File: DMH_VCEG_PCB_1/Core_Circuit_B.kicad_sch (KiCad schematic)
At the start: 98 parts, among them Q1 BC558, Q2 BC548, Q3 BC548, SW1 SW_DPDT_x2, U1 TL074, U2 4001, U3 40106, U4 CD4066BE, U5 TL074, U6 TL074, U7 TL074

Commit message: Placed Circuit B pages
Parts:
- renumbered C18 to C33, C17 to C34, C19 to C35, C20 to C36, C21 to C37, C22 to C38, C24 to C39, C25 to C40, C23 to C41, D3 to D15, D4 to D16, D5 to D17, D6 to D18, D7 to D19, D8 to D20, Q2 to Q5, Q1 to Q6, Q3 to Q7, R73 to R10, R75 to R12, R77 to R14, R74 to R16, R79 to R17, R76 to R18, R101 to R19, R80 to R20, R82 to R21, R100 to R22, R86 to R23, R99 to R24, R81 to R25, R93 to R26, R83 to R27, R98 to R28, R84 to R29, R97 to R30, R95 to R31, R103 to R32, R102 to R33, R91 to R34, R90 to R35, R89 to R36, R94 to R37, R96 to R38, R88 to R39, R92 to R40, R109 to R41, R104 to R42, R105 to R43, R110 to R44, R87 to R45, R106 to R46, R111 to R47, R112 to R48, R107 to R49, R108 to R50, R113 to R51, R114 to R52, R115 to R53, R85 to R54, R72 to R7, R78 to R8, RV23 to RV31, RV25 to RV32, RV26 to RV33, RV19 to RV34, RV18 to RV35, RV20 to RV36, RV27 to RV37, RV21 to RV38, RV24 to RV39, RV22 to RV40, RV17 to RV41, RV28 to RV42, RV29 to RV43, RV30 to RV44, SW1 to SW3, U1 to U11, U4 to U12, U6 to U13, U3 to U14, U2 to U15, U5 to U16, U7 to U17
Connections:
- net Att Logic: now also U12.5, U15.12, U15.4, U15.8; no longer U12.13, U15.1, U15.1, U15.3
- net Dec Logic: now also U15.10; no longer U15.3
- net GND: now also U13.10 (+), U13.5 (+), U17.5 (+); no longer U13.3 (+), U13.3 (+), U17.3 (+)
- net Main Cap: now also U12.4, U12.8; no longer U12.1, U12.1
- net Rel Logic: now also U12.6, U15.11; no longer U12.13, U15.3
- net Sus Level: now also U13.13 (-), U13.14; no longer U13.1, U13.2 (-)
- net at C41.2, R54.2, RV41.1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: now also U16.12 (+); no longer U16.3 (+)
- net at D17.2 (A), U14.2: now also U14.13, U15.9; no longer U14.1, U15.2
- net at Q7.1 (C): now also U12.9; no longer U12.2
- net at R26.1, R28.1, R30.2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: now also U13.6 (-); no longer U13.2 (-)
- net at C39.1, C40.1, R33.1: now also U16.5 (+); no longer U16.3 (+)
- net at R22.1, R23.1, R24.2: now also U13.9 (-); no longer U13.2 (-)
- net at C34.1, R10.1, R16.2: now also U11.5 (+); no longer U11.3 (+)
- net at R46.1, R49.1, R50.2: now also U17.6 (-); no longer U17.2 (-)
- net at C33.2, R12.1, R18.2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: now also U11.6 (-); no longer U11.2 (-)
- net at R24.1, R26.2: now also U13.7; no longer U13.1
- net at R19.1, R22.2: now also U13.8; no longer U13.1
- net at R43.1, R46.2: now also U17.7; no longer U17.1
- net at D19.1 (K), R32.2: now also U13.12 (+); no longer U13.3 (+)
- net at U15.3: now also U15.5; no longer U15.1
- net at C38.2, D18.1 (K), R29.2: now also U15.6; no longer U15.2
- net at Q6.1 (C): now also U12.3; no longer U12.2
- net at C34.2, D15.2 (A), R16.1: now also U11.7; no longer U11.1
- net at D18.2 (A): now also U16.8; no longer U16.1
- new net: R45.2, U16.10 (+), U16.6 (-), U16.7
- new net: Q6.3 (E), U16.13 (-), U16.14, U16.9 (-)
- new net: U14.12, U15.13

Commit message: Reanotated schematic
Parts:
- SW2: renamed from SW3; footprint (none) -> SynthStuff:Toggle_Switch_2_Poles_TE
- U11: footprint (none) -> Package_DIP:DIP-14_W7.62mm_Socket
- U12: renamed from U17; footprint (none) -> Package_DIP:DIP-14_W7.62mm_Socket
- U14: renamed from U13; footprint (none) -> Package_DIP:DIP-14_W7.62mm_Socket
- U15: renamed from U14; footprint (none) -> Package_DIP:DIP-14_W7.62mm_Socket
- U16: renamed from U15; footprint (none) -> Package_DIP:DIP-14_W7.62mm_Socket
- U17: renamed from U16; footprint (none) -> Package_DIP:DIP-14_W7.62mm_Socket
- renumbered C33 to C12, C34 to C13, C35 to C14, C36 to C15, C37 to C16, C38 to C17, C39 to C18, C40 to C19, C41 to C20, R31 to R100, R32 to R101, R33 to R102, R34 to R103, R35 to R104, R36 to R105, R37 to R106, R38 to R107, R39 to R108, R40 to R109, R41 to R110, R42 to R111, R43 to R112, R44 to R113, R45 to R114, R46 to R115, R47 to R116, R48 to R117, R49 to R118, R50 to R119, R51 to R120, R52 to R121, R53 to R122, R54 to R123, R7 to R80, R8 to R81, R10 to R82, R12 to R83, R14 to R84, R16 to R85, R17 to R86, R18 to R87, R19 to R88, R20 to R89, R21 to R90, R22 to R91, R23 to R92, R24 to R93, R25 to R94, R26 to R95, R27 to R96, R28 to R97, R29 to R98, R30 to R99, U12 to U13, U14 to U15, U15 to U16, U16 to U17

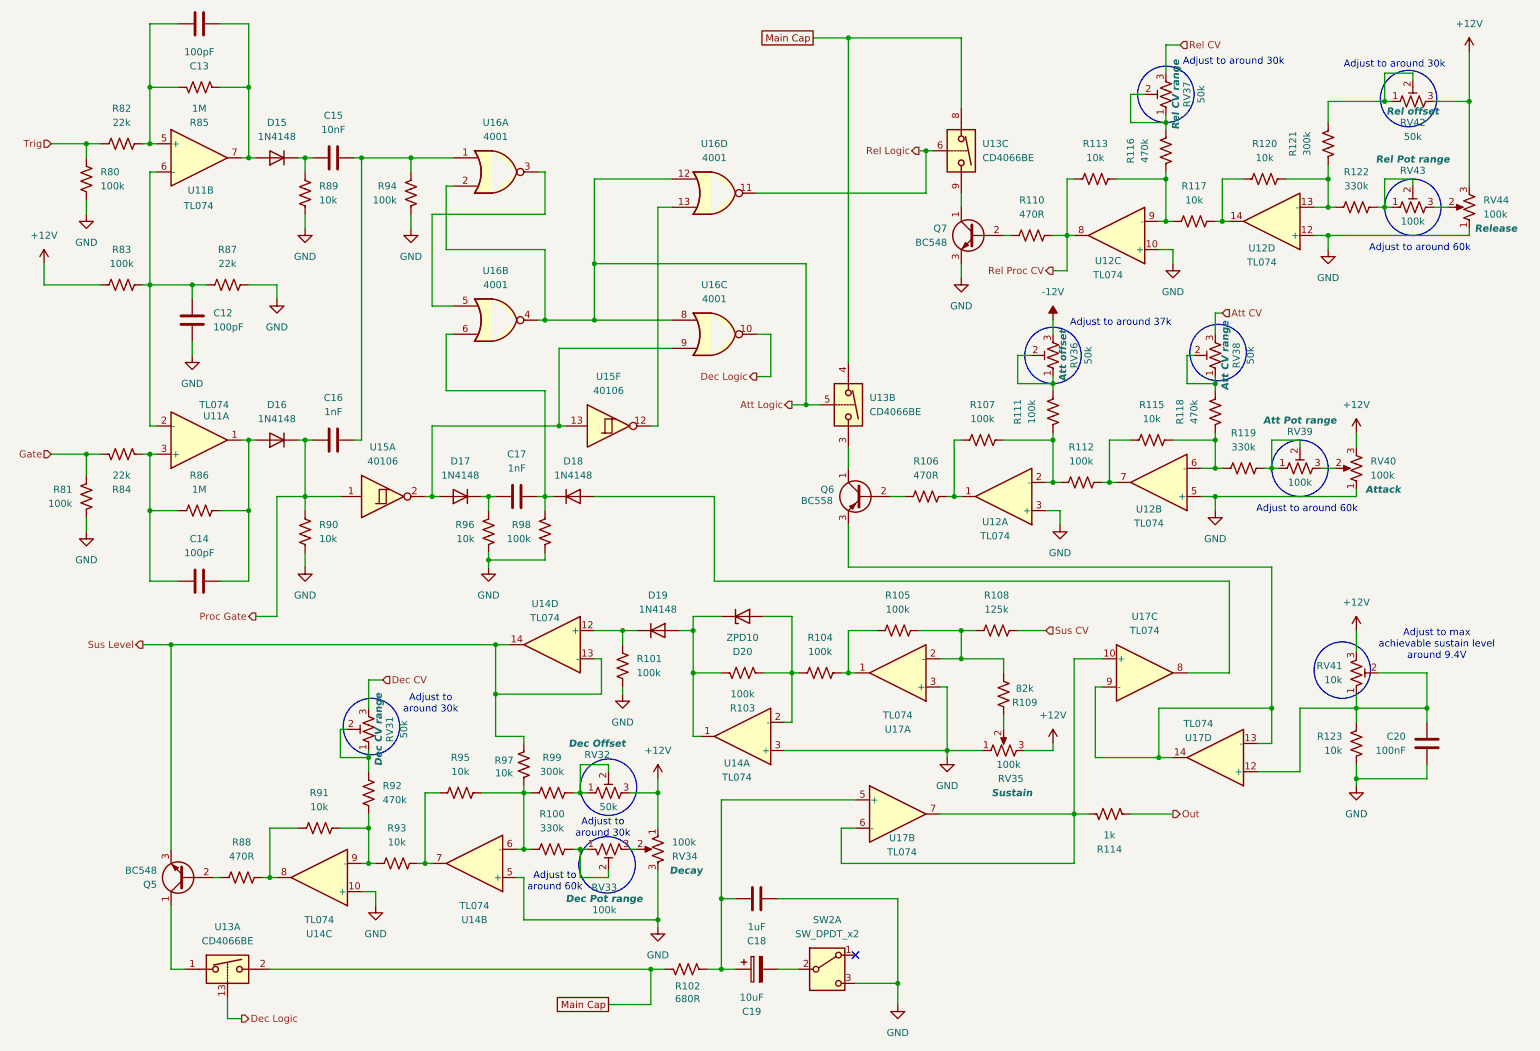
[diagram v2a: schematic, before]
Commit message: Reannotated ICs to match MFOS schematic
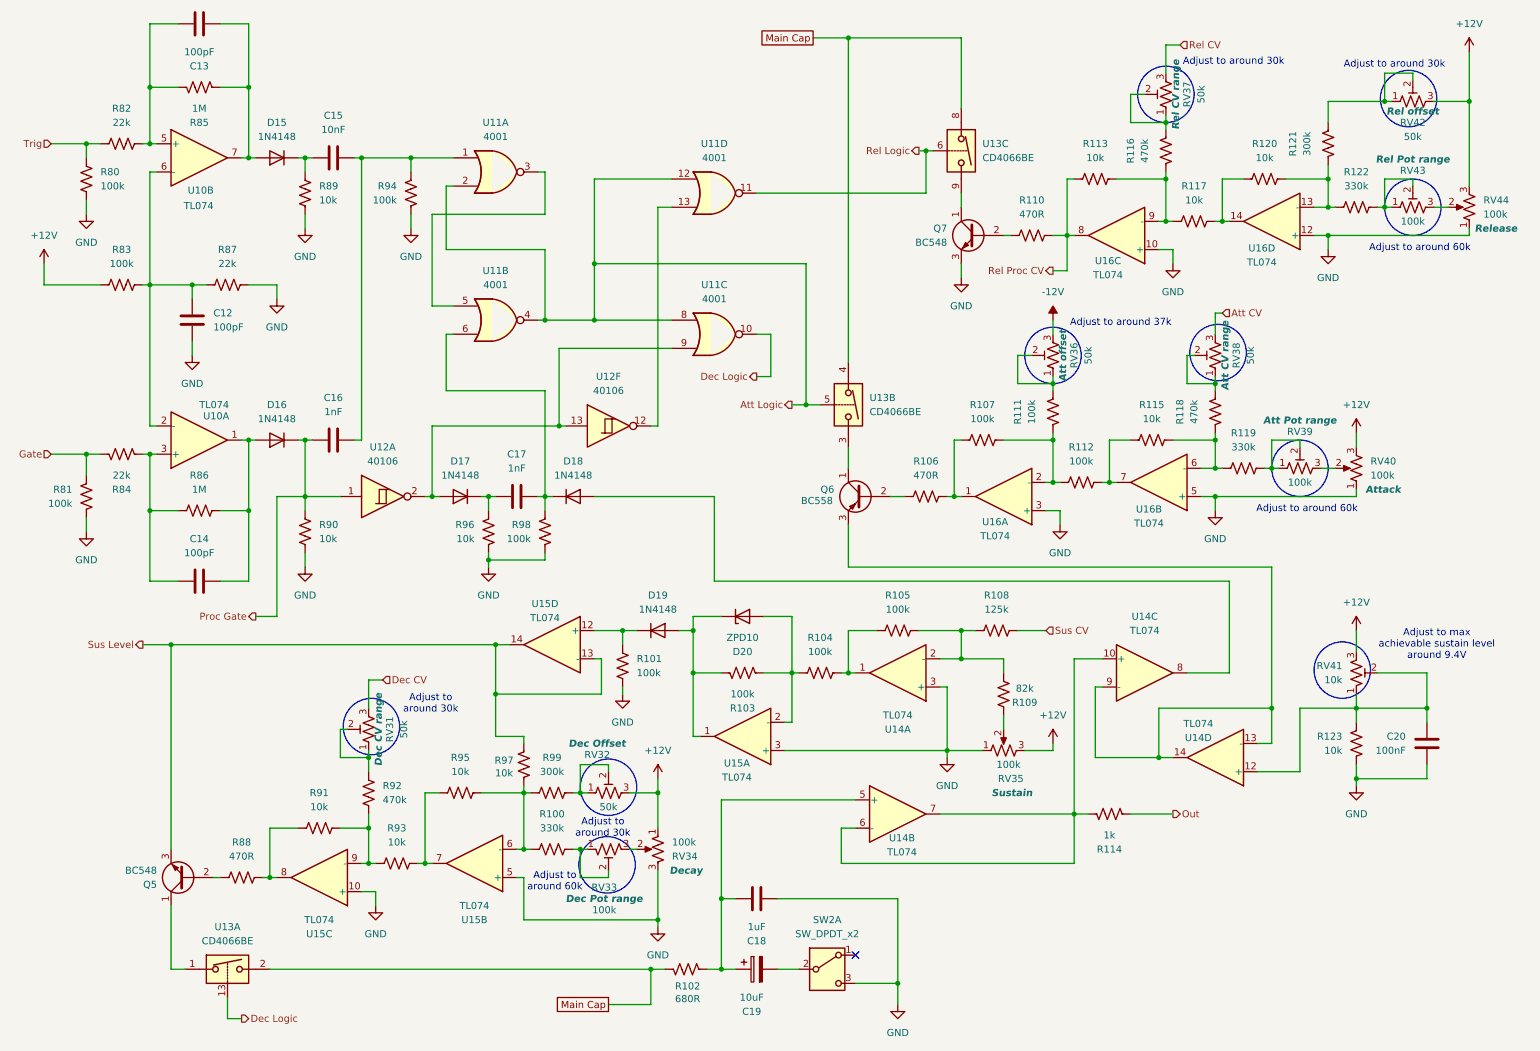
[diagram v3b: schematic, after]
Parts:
- renumbered U11 to U10, U16 to U11, U15 to U12, U17 to U14, U14 to U15, U12 to U16
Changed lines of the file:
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@@
 		(on_board yes)
 		(dnp no)
-		(property "Reference" "U15"
+		(property "Reference" "U12"
 			(at 78.74 90.17 0)
 			(effects
@@
 			)
 		)
+		(property "Function" ""
+			(at 78.74 99.06 0)
+			(effects
+				(font
+					(size 1.27 1.27)
+				)
+			)
+		)
 		(pin "4"
 		)
@@
 			(project "DMH_VCEG_PCB_1"
 				(path "/58f4306d-5387-4983-bb08-41a2313fd315/0347d444-b732-4d51-a48d-f043a0c0fe84"
-					(reference "U15")
+					(reference "U12")
 					(unit 1)
 				)
@@
 		(on_board yes)
 		(dnp no)
-		(property "Reference" "U17"
+		(property "Reference" "U14"
 			(at 172.212 160.528 0)
 			(effects
@@
 			(project "DMH_VCEG_PCB_1"
 				(path "/58f4306d-5387-4983-bb08-41a2313fd315/0347d444-b732-4d51-a48d-f043a0c0fe84"
-					(reference "U17")
+					(reference "U14")
 					(unit 2)
 				)
@@
 		(dnp no)
 		(fields_autoplaced yes)
-		(property "Reference" "U16"
+		(property "Reference" "U11"
 			(at 138.43 60.96 0)
 			(effects
@@
 			)
 		)
+		(property "Function" ""
+			(at 138.43 69.85 0)
+			(effects
+				(font
+					(size 1.27 1.27)
+				)
+			)
+		)
 		(pin "9"
 		)
@@
 			(project "DMH_VCEG_PCB_1"
 				(path "/58f4306d-5387-4983-bb08-41a2313fd315/0347d444-b732-4d51-a48d-f043a0c0fe84"
-					(reference "U16")
+					(reference "U11")
 					(unit 3)
 				)
@@
 		(dnp no)
 		(fields_autoplaced yes)
-		(property "Reference" "U16"
+		(property "Reference" "U11"
 			(at 99.06 58.42 0)
 			(effects
@@
 			)
 		)
+		(property "Function" ""
+			(at 99.06 67.31 0)
+			(effects
+				(font
+					(size 1.27 1.27)
+				)
+			)
+		)
 		(pin "9"
 		)
@@
 			(project "DMH_VCEG_PCB_1"
 				(path "/58f4306d-5387-4983-bb08-41a2313fd315/0347d444-b732-4d51-a48d-f043a0c0fe84"
-					(reference "U16")
+					(reference "U11")
 					(unit 2)
 				)
@@
 		(on_board yes)
 		(dnp no)
-		(property "Reference" "U14"
+		(property "Reference" "U15"
 			(at 107.95 118.364 0)
 			(effects
@@
 			(project "DMH_VCEG_PCB_1"
 				(path "/58f4306d-5387-4983-bb08-41a2313fd315/0347d444-b732-4d51-a48d-f043a0c0fe84"
-					(reference "U14")
+					(reference "U15")
 					(unit 4)
 				)
@@
 		(dnp no)
 		(fields_autoplaced yes)
-		(property "Reference" "U16"
+		(property "Reference" "U11"
 			(at 99.06 31.75 0)
 			(effects
@@
 			)
 		)
+		(property "Function" ""
+			(at 99.06 40.64 0)
+			(effects
+				(font
+					(size 1.27 1.27)
+				)
+			)
+		)
 		(pin "3"
 		)
@@
 			(project "DMH_VCEG_PCB_1"
 				(path "/58f4306d-5387-4983-bb08-41a2313fd315/0347d444-b732-4d51-a48d-f043a0c0fe84"
-					(reference "U16")
+					(reference "U11")
 					(unit 1)
 				)
@@
 		(on_board yes)
 		(dnp no)
-		(property "Reference" "U14"
+		(property "Reference" "U15"
 			(at 67.31 177.8 0)
 			(effects
@@
 			(project "DMH_VCEG_PCB_1"
 				(path "/58f4306d-5387-4983-bb08-41a2313fd315/0347d444-b732-4d51-a48d-f043a0c0fe84"
-					(reference "U14")
+					(reference "U15")
 					(unit 3)
 				)
@@
 		(on_board yes)
 		(dnp no)
-		(property "Reference" "U14"
+		(property "Reference" "U15"
 			(at 142.494 147.066 0)
 			(effects
@@
 			(project "DMH_VCEG_PCB_1"
 				(path "/58f4306d-5387-4983-bb08-41a2313fd315/0347d444-b732-4d51-a48d-f043a0c0fe84"
-					(reference "U14")
+					(reference "U15")
 					(unit 1)
 				)
@@
 		(on_board yes)
 		(dnp no)
-		(property "Reference" "U11"
+		(property "Reference" "U10"
 			(at 45.974 43.942 0)
 			(effects
@@
 			(project "DMH_VCEG_PCB_1"
 				(path "/58f4306d-5387-4983-bb08-41a2313fd315/0347d444-b732-4d51-a48d-f043a0c0fe84"
-					(reference "U11")
+					(reference "U10")
 					(unit 2)
 				)
@@
 		(on_board yes)
 		(dnp no)
-		(property "Reference" "U17"
+		(property "Reference" "U14"
 			(at 225.552 142.494 0)
 			(effects
@@
 			(project "DMH_VCEG_PCB_1"
 				(path "/58f4306d-5387-4983-bb08-41a2313fd315/0347d444-b732-4d51-a48d-f043a0c0fe84"
-					(reference "U17")
+					(reference "U14")
 					(unit 4)
 				)
@@
 		(on_board yes)
 		(dnp no)
-		(property "Reference" "U14"
+		(property "Reference" "U15"
 			(at 95.25 175.26 0)
 			(effects
@@
 			(project "DMH_VCEG_PCB_1"
 				(path "/58f4306d-5387-4983-bb08-41a2313fd315/0347d444-b732-4d51-a48d-f043a0c0fe84"
-					(reference "U14")
+					(reference "U15")
 					(unit 2)
 				)
@@
 		(on_board yes)
 		(dnp no)
-		(property "Reference" "U12"
+		(property "Reference" "U16"
 			(at 209.296 56.642 0)
 			(effects
@@
 			(project "DMH_VCEG_PCB_1"
 				(path "/58f4306d-5387-4983-bb08-41a2313fd315/0347d444-b732-4d51-a48d-f043a0c0fe84"
-					(reference "U12")
+					(reference "U16")
 					(unit 3)
 				)
@@
 		(on_board yes)
 		(dnp no)
-		(property "Reference" "U12"
+		(property "Reference" "U16"
 			(at 236.982 54.356 0)
 			(effects
@@
 			(project "DMH_VCEG_PCB_1"
 				(path "/58f4306d-5387-4983-bb08-41a2313fd315/0347d444-b732-4d51-a48d-f043a0c0fe84"
-					(reference "U12")
+					(reference "U16")
 					(unit 4)
 				)
@@
 		(dnp no)
 		(fields_autoplaced yes)
-		(property "Reference" "U16"
+		(property "Reference" "U11"
 			(at 138.43 35.56 0)
 			(effects
@@
 			)
 		)
+		(property "Function" ""
+			(at 138.43 44.45 0)
+			(effects
+				(font
+					(size 1.27 1.27)
+				)
+			)
+		)
 		(pin "9"
 		)
@@
 			(project "DMH_VCEG_PCB_1"
 				(path "/58f4306d-5387-4983-bb08-41a2313fd315/0347d444-b732-4d51-a48d-f043a0c0fe84"
-					(reference "U16")
+					(reference "U11")
 					(unit 4)
 				)
@@
 		(on_board yes)
 		(dnp no)
-		(property "Reference" "U12"
+		(property "Reference" "U16"
 			(at 188.976 103.632 0)
 			(effects
@@
 			(project "DMH_VCEG_PCB_1"
 				(path "/58f4306d-5387-4983-bb08-41a2313fd315/0347d444-b732-4d51-a48d-f043a0c0fe84"
-					(reference "U12")
+					(reference "U16")
 					(unit 1)
 				)
@@
 		(on_board yes)
 		(dnp no)
-		(property "Reference" "U11"
+		(property "Reference" "U10"
 			(at 48.768 84.582 0)
 			(effects
@@
 			(project "DMH_VCEG_PCB_1"
 				(path "/58f4306d-5387-4983-bb08-41a2313fd315/0347d444-b732-4d51-a48d-f043a0c0fe84"
-					(reference "U11")
+					(reference "U10")
 					(unit 1)
 				)
@@
 		(dnp no)
 		(fields_autoplaced yes)
-		(property "Reference" "U17"
+		(property "Reference" "U14"
 			(at 215.9 120.65 0)
 			(effects
@@
 			(project "DMH_VCEG_PCB_1"
 				(path "/58f4306d-5387-4983-bb08-41a2313fd315/0347d444-b732-4d51-a48d-f043a0c0fe84"
-					(reference "U17")
+					(reference "U14")
 					(unit 3)
 				)
@@
 		(on_board yes)
 		(dnp no)
-		(property "Reference" "U12"
+		(property "Reference" "U16"
 			(at 216.662 101.346 0)
 			(effects
@@
 			(project "DMH_VCEG_PCB_1"
 				(path "/58f4306d-5387-4983-bb08-41a2313fd315/0347d444-b732-4d51-a48d-f043a0c0fe84"
-					(reference "U12")
+					(reference "U16")
 					(unit 2)
 				)
@@
 		(on_board yes)
 		(dnp no)
-		(property "Reference" "U17"
+		(property "Reference" "U14"
 			(at 171.45 140.97 0)
 			(effects
@@
 			(project "DMH_VCEG_PCB_1"
 				(path "/58f4306d-5387-4983-bb08-41a2313fd315/0347d444-b732-4d51-a48d-f043a0c0fe84"
-					(reference "U17")
+					(reference "U14")
 					(unit 1)
 				)
@@
 		(dnp no)
 		(fields_autoplaced yes)
-		(property "Reference" "U15"
+		(property "Reference" "U12"
 			(at 119.38 77.47 0)
 			(effects
@@
 			)
 		)
+		(property "Function" ""
+			(at 119.38 86.36 0)
+			(effects
+				(font
+					(size 1.27 1.27)
+				)
+			)
+		)
 		(pin "10"
 		)
@@
 			(project "DMH_VCEG_PCB_1"
 				(path "/58f4306d-5387-4983-bb08-41a2313fd315/0347d444-b732-4d51-a48d-f043a0c0fe84"
-					(reference "U15")
+					(reference "U12")
 					(unit 6)
 				)

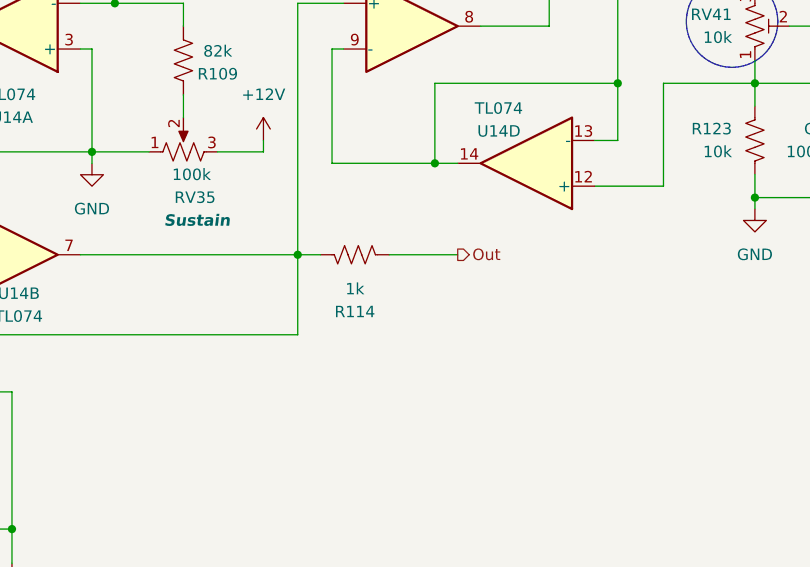
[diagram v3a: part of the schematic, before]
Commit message: Fixed inverted Out and some fp assignments
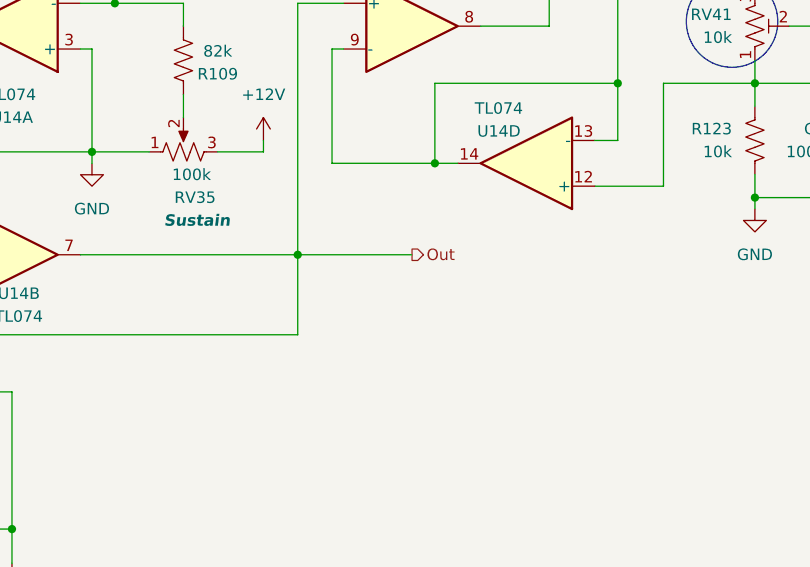
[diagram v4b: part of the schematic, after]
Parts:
- removed R114: 1k, Resistor_THT:R_Axial_DIN0207_L6.3mm_D2.5mm_P7.62mm_Horizontal, symbol Device:R_US
- C12, C13, C14: footprint Capacitor_THT:C_Disc_D4.3mm_W1.9mm_P5.00mm -> Capacitor_THT:C_Disc_D3.8mm_W2.6mm_P2.50mm
- D20: footprint Diode_THT:D_DO-35_SOD27_P10.16mm_Horizontal -> Diode_THT:D_DO-35_SOD27_P7.62mm_Horizontal
- Q6: footprint Package_TO_SOT_THT:TO-92_Inline -> Package_TO_SOT_THT:TO-92L_Inline_Wide
- RV34, RV35: footprint SynthStuff:Potentiometer_TT_P110KH1 -> SynthStuff:Potentiometer_Alpha_RD901F-40-00D_Single_Vertical
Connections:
- net Out: now also U14.10 (+), U14.6 (-), U14.7
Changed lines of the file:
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@@
 	(wire
 		(pts
-			(xy 203.2 156.21) (xy 205.74 156.21)
+			(xy 203.2 156.21) (xy 215.9 156.21)
 		)
 		(stroke
@@
 	(wire
 		(pts
-			(xy 213.36 156.21) (xy 220.98 156.21)
-		)
-		(stroke
-			(width 0)
-			(type default)
-		)
-	)
-	(wire
-		(pts
 			(xy 203.2 165.1) (xy 203.2 156.21)
 		)
@@
 	(hierarchical_label "Out"
 		(shape output)
-		(at 220.98 156.21 0)
+		(at 215.9 156.21 0)
 		(effects
 			(font
@@
 			)
 		)
-		(property "Footprint" "Capacitor_THT:C_Disc_D4.3mm_W1.9mm_P5.00mm"
+		(property "Footprint" "Capacitor_THT:C_Disc_D3.8mm_W2.6mm_P2.50mm"
 			(at 43.4848 63.5 0)
 			(effects
@@
 			)
 		)
-		(property "Footprint" "Capacitor_THT:C_Disc_D4.3mm_W1.9mm_P5.00mm"
+		(property "Footprint" "Capacitor_THT:C_Disc_D3.8mm_W2.6mm_P2.50mm"
 			(at 49.53 113.3348 0)
 			(effects
@@
 			)
 		)
-		(property "Footprint" "Package_TO_SOT_THT:TO-92_Inline"
+		(property "Footprint" "Package_TO_SOT_THT:TO-92L_Inline_Wide"
 			(at 160.02 100.965 0)
 			(effects
@@
 	)
 	(symbol
-		(lib_id "Device:R_US")
-		(at 209.55 156.21 270)
-		(mirror x)
-		(unit 1)
-		(exclude_from_sim no)
-		(in_bom yes)
-		(on_board yes)
-		(dnp no)
-		(property "Reference" "R114"
-			(at 209.55 162.56 90)
-			(effects
-				(font
-					(size 1.27 1.27)
-				)
-			)
-		)
-		(property "Value" "1k"
-			(at 209.55 160.02 90)
-			(effects
-				(font
-					(size 1.27 1.27)
-				)
-			)
-		)
-		(property "Footprint" "Resistor_THT:R_Axial_DIN0207_L6.3mm_D2.5mm_P7.62mm_Horizontal"
-			(at 209.296 155.194 90)
-			(effects
-				(font
-					(size 1.27 1.27)
-				)
-				(hide yes)
-			)
-		)
-		(property "Datasheet" "~"
-			(at 209.55 156.21 0)
-			(effects
-				(font
-					(size 1.27 1.27)
-				)
-				(hide yes)
-			)
-		)
-		(property "Description" "Resistor, US symbol"
-			(at 209.55 156.21 0)
-			(effects
-				(font
-					(size 1.27 1.27)
-				)
-				(hide yes)
-			)
-		)
-		(pin "2"
-		)
-		(pin "1"
-		)
-		(instances
-			(project "DMH_VCEG_PCB_1"
-				(path "/58f4306d-5387-4983-bb08-41a2313fd315/0347d444-b732-4d51-a48d-f043a0c0fe84"
-					(reference "R114")
-					(unit 1)
-				)
-			)
-		)
-	)
-	(symbol
 		(lib_id "power:GND")
 		(at 44.45 73.66 0)
@@
 		(exclude_from_sim no)
 		(in_bom yes)
-		(on_board no)
+		(on_board yes)
 		(dnp no)
 		(property "Reference" "RV34"
@@
 			)
 		)
-		(property "Footprint" "SynthStuff:Potentiometer_TT_P110KH1"
+		(property "Footprint" "SynthStuff:Potentiometer_Alpha_RD901F-40-00D_Single_Vertical"
 			(at 128.27 162.56 0)
 			(effects
@@
 			)
 		)
-		(property "Footprint" "Diode_THT:D_DO-35_SOD27_P10.16mm_Horizontal"
+		(property "Footprint" "Diode_THT:D_DO-35_SOD27_P7.62mm_Horizontal"
 			(at 143.51 116.205 0)
 			(effects
@@
 			)
 		)
-		(property "Footprint" "Capacitor_THT:C_Disc_D4.3mm_W1.9mm_P5.00mm"
+		(property "Footprint" "Capacitor_THT:C_Disc_D3.8mm_W2.6mm_P2.50mm"
 			(at 49.53 14.9352 0)
 			(effects
@@
 		(exclude_from_sim no)
 		(in_bom yes)
-		(on_board no)
+		(on_board yes)
 		(dnp no)
 		(property "Reference" "RV35"
@@
 			)
 		)
-		(property "Footprint" "SynthStuff:Potentiometer_TT_P110KH1"
+		(property "Footprint" "SynthStuff:Potentiometer_Alpha_RD901F-40-00D_Single_Vertical"
 			(at 190.5 144.78 0)
 			(effects
